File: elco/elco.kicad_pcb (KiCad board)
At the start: 2 copper layers, 18 x 33.5 mm, 4 parts

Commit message: Elco board
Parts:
- removed REF** (x2): PinHeader_1x02_P1.27mm_Vertical, Connector_PinHeader_1.27mm:PinHeader_1x02_P1.27mm_Vertical
- removed REF** (x2): PinHeader_1x06_P1.27mm_Vertical, Connector_PinHeader_1.27mm:PinHeader_1x06_P1.27mm_Vertical
- added C1: 1u, Capacitor_SMD:C_0805_2012Metric, B.Cu at (74.2, 57.4)
- added C2: 1u, Capacitor_SMD:C_0805_2012Metric, B.Cu at (78.0, 57.4)
- added D1: LED_Dual_Bidirectional, LED_THT:LED_D5.0mm, F.Cu at (64.8, 43.2)
- added D2: LED_Dual_Bidirectional, LED_THT:LED_D5.0mm, F.Cu at (87.6, 43.2)
- added F1: Fuse, Fuse:Fuseholder_Clip-5x20mm_Bel_FC-203-22_Lateral_P17.80x5.00mm_D1.17mm_Horizontal, B.Cu at (95.2, 99.1)
- added J1: ~, ELCO:ELCO, F.Cu at (76.2, 76.2)
- added J2: Motor / Power, Connector_PinHeader_2.54mm:PinHeader_2x14_P2.54mm_Vertical, B.Cu at (91.4, 76.6)
- added J3: IO, Connector_PinHeader_2.54mm:PinHeader_2x17_P2.54mm_Vertical, B.Cu at (56.6, 84.8)
- added J4: Barrel_Jack_MountingPin, Connector_BarrelJack:BarrelJack_CUI_PJ-063AH_Horizontal, B.Cu at (61.0, 89.8)
- added R1: 10k, Resistor_SMD:R_0805_2012Metric, B.Cu at (74.2, 48.8)
- added R2: 2k49, Resistor_SMD:R_0805_2012Metric, B.Cu at (78.0, 48.8)
- added R3: 330, Resistor_SMD:R_0805_2012Metric, B.Cu at (70.6, 41.1)
- added R4: 330, Resistor_SMD:R_0805_2012Metric, B.Cu at (70.6, 45.2)
- added R5: 330, Resistor_SMD:R_0805_2012Metric, B.Cu at (81.8, 41.1)
- added R6: 330, Resistor_SMD:R_0805_2012Metric, B.Cu at (81.8, 45.2)
- added R7: 5k, Resistor_SMD:R_0805_2012Metric, B.Cu at (68.8, 48.8)
- added SW1: SW_DPDT_x2, Button_Switch_THT:SW_NKK_G1xJP, F.Cu at (74.9, 40.6)
- added U1: TPSM53602RDA, Package_DFN_QFN:Texas_B3QFN-14-1EP_5x5.5mm_P0.65mm_ThermalVia, B.Cu at (76.2, 53.1)
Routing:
- net (no net): vias 38 -> 0
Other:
- board size 18 x 33.5 mm -> 43.2 x 63.5 mm

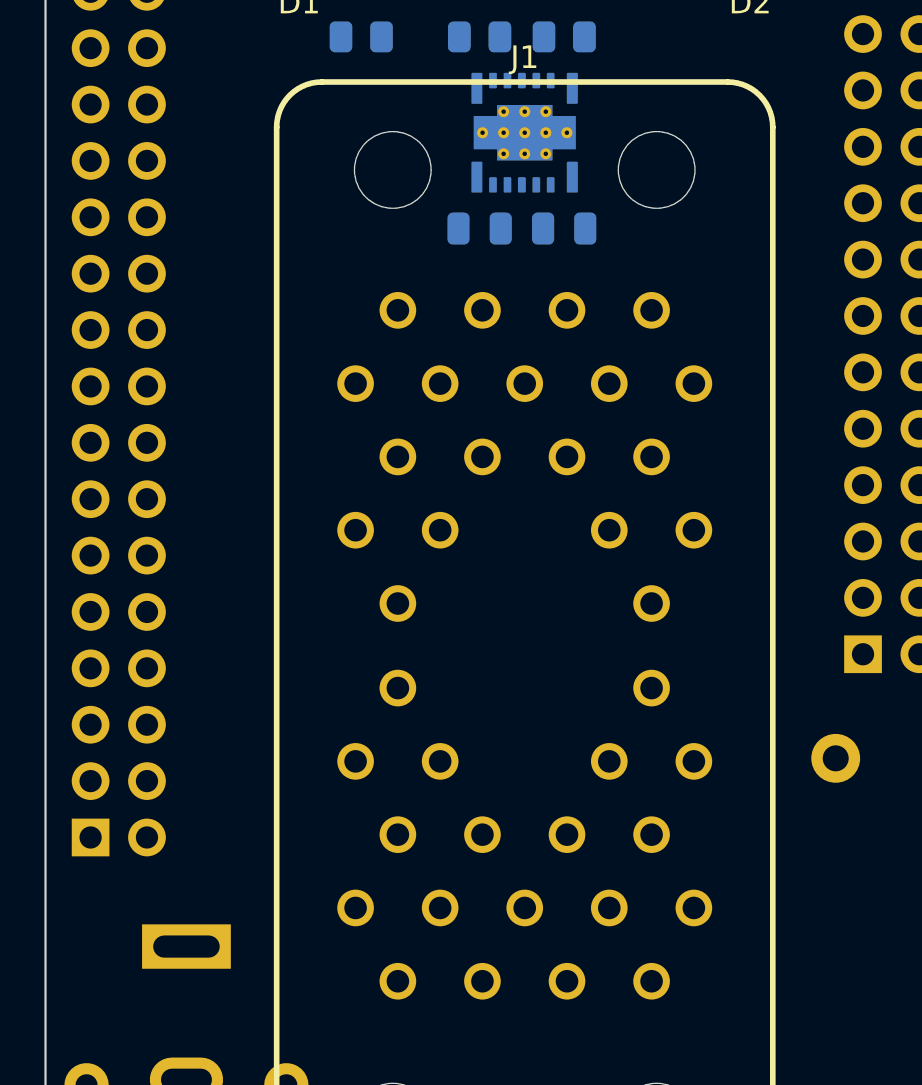
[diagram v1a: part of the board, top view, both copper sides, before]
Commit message: ELCO routing
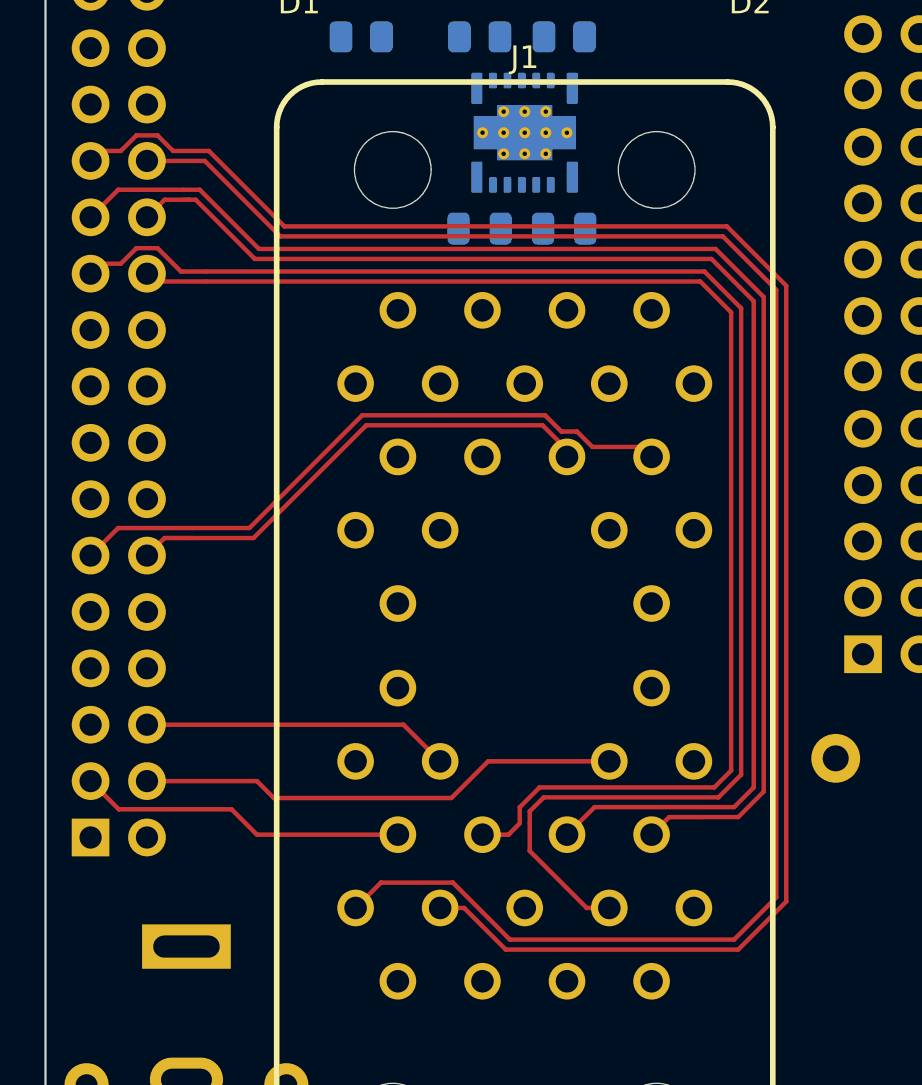
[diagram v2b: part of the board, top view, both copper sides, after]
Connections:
- net Hall_I_In renamed Hall_I
- net Lim_Aux_In renamed Lim_Aux
- J1 pad AA: unconnected-(J1-HALL_A-PadAA) -> Hall_A
- J1 pad BB: unconnected-(J1-HALL_B-PadBB) -> Hall_B
- J1 pad DD: unconnected-(J1-HALL_C-PadDD) -> Hall_C
- J1 pad EE: unconnected-(J1-ENC_A--PadEE) -> Enc_A-
- J1 pad F: PH1 -> PH3
- J1 pad FF: unconnected-(J1-ENC_B--PadFF) -> Enc_B-
- J1 pad HH: unconnected-(J1-ENC_B+-PadHH) -> Enc_B+
- J1 pad J: PH2 -> PH4
- J1 pad JJ: unconnected-(J1-ENC_I--PadJJ) -> Enc_I-
- J1 pad KK: unconnected-(J1-ENC_I+-PadKK) -> Enc_I+
- J1 pad L: unconnected-(J1-AUX_B+-PadL) -> Aux_Enc_B+
- J1 pad LL: unconnected-(J1-GND-PadLL) -> GND
- J1 pad M: unconnected-(J1-AUX_B--PadM) -> Aux_Enc_B-
- J1 pad MM: unconnected-(J1-ENC_A+-PadMM) -> Enc_A+
- J1 pad N: unconnected-(J1-AUX_A+-PadN) -> Aux_Enc_A+
- J1 pad P: unconnected-(J1-AUX_A--PadP) -> Aux_Enc_A-
- J1 pad RR: unconnected-(J1-LIM_F-PadRR) -> Lim_L
- J1 pad S: PH3 -> PH1
- J1 pad T: PH4 -> PH2
- J1 pad TT: unconnected-(J1-LIM_R-PadTT) -> Lim_R
- J1 pad W: unconnected-(J1-HOME-PadW) -> Lim_H
- J3 pad 10: Aux_Enc_B_In+ -> Aux_Enc_B+
- J3 pad 11: Aux_Enc_A_In- -> Aux_Enc_A-
- J3 pad 12: Aux_Enc_A_In+ -> Aux_Enc_A+
- J3 pad 21: Enc_A_In+ -> Enc_A+
- J3 pad 22: Enc_A_In- -> Enc_A-
- J3 pad 23: Enc_B_In+ -> Enc_B+
- J3 pad 24: Enc_B_In- -> Enc_B-
- J3 pad 25: Enc_I_In+ -> Enc_I+
- J3 pad 26: Enc_I_In- -> Enc_I-
- J3 pad 29: Lim_L_In -> Lim_L
- J3 pad 3: Hall_C_In -> Hall_C
- J3 pad 30: Lim_H_In -> Lim_H
- J3 pad 31: Lim_R_In -> Lim_R
- J3 pad 4: Hall_B_In -> Hall_B
- J3 pad 6: Hall_A_In -> Hall_A
- J3 pad 9: Aux_Enc_B_In- -> Aux_Enc_B-
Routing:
- net Enc_I+: track 0.00 -> 79.6 mm
- net Enc_I-: track 0.00 -> 79.4 mm
- net Enc_A+: track 0.00 -> 68.6 mm
- net Enc_B-: track 0.00 -> 61.0 mm
- net Enc_B+: track 0.00 -> 61.0 mm
- net Enc_A-: track 0.00 -> 60.5 mm
- net Aux_Enc_A-: track 0.00 -> 28.7 mm
- net Aux_Enc_A+: track 0.00 -> 22.1 mm
- net Hall_B: track 0.00 -> 21.8 mm
- net Hall_C: track 0.00 -> 14.8 mm
- net Hall_A: track 0.00 -> 13.9 mm
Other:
- copper layers 2 -> 4

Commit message: Getting ready for fab
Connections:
- J1 pad F: PH3 -> PH4
- J1 pad J: PH4 -> PH3
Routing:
- net Lim_R: track 0.00 -> 63.7 mm
- net Lim_L: track 0.00 -> 56.6 mm
- net Lim_H: track 0.00 -> 46.9 mm, vias 0 -> 1
- net Aux_Enc_B-: track 0.00 -> 21.5 mm
- net Aux_Enc_B+: track 0.00 -> 14.8 mm
- added copper zone on In1.Cu, net GND
- added copper zone on B.Cu, net PH1
- added copper zone on B.Cu, net PH2
- added copper zone on B.Cu, net PH3
- added copper zone on B.Cu, net PH4
- added copper zone on In2.Cu, net Vdrive
